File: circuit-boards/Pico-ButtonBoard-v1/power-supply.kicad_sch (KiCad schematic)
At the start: 28 parts, among them Q1 BSS123, Q2 BSS123, U2 TPS54202DDC, U6 ITS41k0S-ME-N

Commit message: Add power over CAN to supply joystick from button interfaces.
Signed-off-by: Scott Berman <sgberman1@gmail.com>
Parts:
- added D12: S1B, Diode_SMD:D_SMA, symbol Pico-ButtonBoard:S1B
- TP1: renamed from TP2; value CAN_RX -> 5V
- TP2: renamed from TP1; value CAN_RX -> VPS
- TP3: value CAN_RX -> VBAT
- renumbered D13 to D14, D16 to D17, D17 to D18, D18 to D19, D22 to D23, D23 to D24, R24 to R23, R23 to R51
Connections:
- net V_PS: now also D12.2 (A); no longer C1.1, R19.2, U2.3 (VIN)
- new net: C1.1, D12.1 (K), R19.2, U2.3 (VIN)
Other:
- note added: "5.18V Setpoint"
- note removed: "5.4V Setpoint"
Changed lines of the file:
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@@
 	(title_block
 		(title "Pico Button Board")
-		(date "2025-12-29")
+		(date "2025-12-30")
 		(rev "1")
 	)
@@
 		)
 	)
-	(text "5.4V Setpoint"
+	(text "5.18V Setpoint"
 		(exclude_from_sim no)
 		(at 279.654 147.32 0)
@@
 	)
 	(junction
+		(at 184.15 96.52)
+		(diameter 0)
+		(color 0 0 0 0)
+	)
+	(junction
 		(at 269.24 137.16)
 		(diameter 0)
@@
 	(wire
 		(pts
+			(xy 184.15 96.52) (xy 184.15 120.65)
+		)
+		(stroke
+			(width 0)
+			(type default)
+		)
+	)
+	(wire
+		(pts
 			(xy 146.05 144.78) (xy 148.59 144.78)
 		)
@@
 	(wire
 		(pts
-			(xy 184.15 93.98) (xy 184.15 120.65)
+			(xy 184.15 93.98) (xy 184.15 96.52)
 		)
 		(stroke
@@
 	(wire
 		(pts
-			(xy 184.15 120.65) (xy 210.82 120.65)
+			(xy 184.15 120.65) (xy 196.85 120.65)
 		)
 		(stroke
@@
 	(wire
 		(pts
+			(xy 184.15 96.52) (xy 349.25 96.52)
+		)
+		(stroke
+			(width 0)
+			(type default)
+		)
+	)
+	(wire
+		(pts
 			(xy 237.49 125.73) (xy 237.49 143.51)
 		)
@@
 	(wire
 		(pts
+			(xy 204.47 120.65) (xy 210.82 120.65)
+		)
+		(stroke
+			(width 0)
+			(type default)
+		)
+	)
+	(wire
+		(pts
 			(xy 102.87 139.7) (xy 102.87 144.78)
 		)
@@
 	)
 	(label "V_PS"
-		(at 193.04 120.65 0)
+		(at 185.42 120.65 0)
 		(effects
 			(font
@@
 		)
 	)
+	(hierarchical_label "V_PS"
+		(shape passive)
+		(at 349.25 96.52 0)
+		(effects
+			(font
+				(size 1.27 1.27)
+			)
+			(justify left)
+		)
+	)
 	(hierarchical_label "+V_BAT"
 		(shape input)
@@
 		(on_board yes)
 		(dnp no)
-		(property "Reference" "D13"
+		(property "Reference" "D14"
 			(at 112.268 152.4 90)
 			(effects
@@
 			(project "Pico-ButtonBoard-v1"
 				(path "/644201a9-3a2f-4df3-9c93-2ae55394df4b/dd046a3a-8e17-4277-b6b1-7e4df1560d2f"
-					(reference "D13")
+					(reference "D14")
 					(unit 1)
 				)
@@
 		(on_board yes)
 		(dnp no)
-		(property "Reference" "D16"
+		(property "Reference" "D17"
 			(at 68.072 117.602 0)
 			(effects
@@
 		)
 		(property "Value" "S1B"
-			(at 72.644 122.174 0)
+			(at 68.58 123.952 0)
 			(effects
 				(font
@@
 			(project ""
 				(path "/644201a9-3a2f-4df3-9c93-2ae55394df4b/dd046a3a-8e17-4277-b6b1-7e4df1560d2f"
-					(reference "D16")
+					(reference "D17")
 					(unit 1)
 				)
@@
 		(on_board yes)
 		(dnp no)
-		(property "Reference" "D17"
+		(property "Reference" "D18"
 			(at 68.072 90.932 0)
 			(effects
@@
 		)
 		(property "Value" "S1B"
-			(at 72.39 96.012 0)
+			(at 68.326 97.79 0)
 			(effects
 				(font
@@
 			(project "Pico-ButtonBoard-v1"
 				(path "/644201a9-3a2f-4df3-9c93-2ae55394df4b/dd046a3a-8e17-4277-b6b1-7e4df1560d2f"
-					(reference "D17")
+					(reference "D18")
+					(unit 1)
+				)
+			)
+		)
+	)
+	(symbol
+		(lib_id "Pico-ButtonBoard:S1B")
+		(at 200.66 120.65 180)
+		(unit 1)
+		(exclude_from_sim no)
+		(in_bom yes)
+		(on_board yes)
+		(dnp no)
+		(property "Reference" "D12"
+			(at 200.152 117.602 0)
+			(effects
+				(font
+					(size 1.27 1.27)
+				)
+			)
+		)
+		(property "Value" "S1B"
+			(at 200.66 123.952 0)
+			(effects
+				(font
+					(size 1.27 1.27)
+				)
+			)
+		)
+		(property "Footprint" "Diode_SMD:D_SMA"
+			(at 200.66 116.205 0)
+			(effects
+				(font
+					(size 1.27 1.27)
+				)
+				(hide yes)
+			)
+		)
+		(property "Datasheet" "Components/onsemi-S1B.pdf"
+			(at 200.66 120.65 0)
+			(effects
+				(font
+					(size 1.27 1.27)
+				)
+				(hide yes)
+			)
+		)
+		(property "Description" "100V, 1A, General Purpose Rectifier Diode, SMA(DO-214AC)"
+			(at 200.66 120.65 0)
+			(effects
+				(font
+					(size 1.27 1.27)
+				)
+				(hide yes)
+			)
+		)
+		(property "MFG" "onsemi"
+			(at 200.66 120.65 0)
+			(effects
+				(font
+					(size 1.27 1.27)
+				)
+				(hide yes)
+			)
+		)
+		(property "MFG P/N" "S1B"
+			(at 200.66 120.65 0)
+			(effects
+				(font
+					(size 1.27 1.27)
+				)
+				(hide yes)
+			)
+		)
+		(property "DIST" "Digikey"
+			(at 200.66 120.65 0)
+			(effects
+				(font
+					(size 1.27 1.27)
+				)
+				(hide yes)
+			)
+		)
+		(property "DIST P/N" "S1BFSCT-ND"
+			(at 200.66 120.65 0)
+			(effects
+				(font
+					(size 1.27 1.27)
+				)
+				(hide yes)
+			)
+		)
+		(pin "1"
+		)
+		(pin "2"
+		)
+		(instances
+			(project "Pico-ButtonBoard-v1"
+				(path "/644201a9-3a2f-4df3-9c93-2ae55394df4b/dd046a3a-8e17-4277-b6b1-7e4df1560d2f"
+					(reference "D12")
 					(unit 1)
 				)
@@
 		(on_board yes)
 		(dnp no)
-		(property "Reference" "D22"
+		(property "Reference" "D23"
 			(at 147.828 152.4 90)
 			(effects
@@
 			(project "Pico-ButtonBoard-v1"
 				(path "/644201a9-3a2f-4df3-9c93-2ae55394df4b/dd046a3a-8e17-4277-b6b1-7e4df1560d2f"
-					(reference "D22")
+					(reference "D23")
 					(unit 1)
 				)
@@
 		)
 		(property "Value" "S1B"
-			(at 339.344 124.714 0)
+			(at 335.28 126.492 0)
 			(effects
 				(font
@@
 			)
 		)
-		(property "Value" "CAN_RX"
+		(property "Value" "VBAT"
 			(at 123.19 118.6179 0)
 			(effects
@@
 		(on_board yes)
 		(dnp yes)
-		(property "Reference" "TP1"
+		(property "Reference" "TP2"
 			(at 184.15 88.646 0)
 			(effects
@@
 			)
 		)
-		(property "Value" "CAN_RX"
+		(property "Value" "VPS"
 			(at 186.69 91.9479 0)
 			(effects
@@
 			(project "Pico-ButtonBoard-v1"
 				(path "/644201a9-3a2f-4df3-9c93-2ae55394df4b/dd046a3a-8e17-4277-b6b1-7e4df1560d2f"
-					(reference "TP1")
+					(reference "TP2")
 					(unit 1)
 				)
@@
 		(on_board yes)
 		(dnp yes)
-		(property "Reference" "TP2"
+		(property "Reference" "TP1"
 			(at 316.23 117.856 0)
 			(effects
@@
 			)
 		)
-		(property "Value" "CAN_RX"
+		(property "Value" "5V"
 			(at 318.77 121.1579 0)
 			(effects
@@
 			(project "Pico-ButtonBoard-v1"
 				(path "/644201a9-3a2f-4df3-9c93-2ae55394df4b/dd046a3a-8e17-4277-b6b1-7e4df1560d2f"
-					(reference "TP2")
+					(reference "TP1")
 					(unit 1)
 				)
@@
 		(on_board yes)
 		(dnp no)
-		(property "Reference" "R23"
+		(property "Reference" "R51"
 			(at 139.954 133.35 90)
 			(effects
@@
 			(project "Pico-ButtonBoard-v1"
 				(path "/644201a9-3a2f-4df3-9c93-2ae55394df4b/dd046a3a-8e17-4277-b6b1-7e4df1560d2f"
-					(reference "R23")
+					(reference "R51")
 					(unit 1)
 				)
@@
 		(on_board yes)
 		(dnp no)
-		(property "Reference" "D18"
+		(property "Reference" "D19"
 			(at 68.072 99.822 0)
 			(effects
@@
 		)
 		(property "Value" "S1B"
-			(at 72.39 104.648 0)
+			(at 68.326 106.426 0)
 			(effects
 				(font
@@
 			(project "Pico-ButtonBoard-v1"
 				(path "/644201a9-3a2f-4df3-9c93-2ae55394df4b/dd046a3a-8e17-4277-b6b1-7e4df1560d2f"
-					(reference "D18")
+					(reference "D19")
 					(unit 1)
 				)
@@
 		(on_board yes)
 		(dnp no)
-		(property "Reference" "D23"
+		(property "Reference" "D24"
 			(at 100.584 134.874 90)
 			(effects
@@
 			(project "Pico-ButtonBoard-v1"
 				(path "/644201a9-3a2f-4df3-9c93-2ae55394df4b/dd046a3a-8e17-4277-b6b1-7e4df1560d2f"
-					(reference "D23")
+					(reference "D24")
 					(unit 1)
 				)
@@
 		(on_board yes)
 		(dnp no)
-		(property "Reference" "R24"
+		(property "Reference" "R23"
 			(at 104.394 157.48 90)
 			(effects
@@
 			(project "Pico-ButtonBoard-v1"
 				(path "/644201a9-3a2f-4df3-9c93-2ae55394df4b/dd046a3a-8e17-4277-b6b1-7e4df1560d2f"
-					(reference "R24")
+					(reference "R23")
 					(unit 1)
 				)

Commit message: Change diodes to schottky. Change 5V setpoint to 5.18V
Signed-off-by: Scott Berman <sgberman1@gmail.com>
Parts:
- D10, D12, D17, D18, D19: value S1B -> B340AE-13; DIST P/N S1BFSCT-ND -> B340AE-13DICT-ND; MFG onsemi -> Diodes Inc; MFG P/N S1B -> B340AE-13
- R18: value 12.4k-1%-0805 -> 13k-1%-0805; DIST P/N RMCF0805FT12K4CT-ND -> A126339CT-ND; MFG Stackpole -> TE Connectivity Passive Product; MFG P/N RMCF0805FT12K4 -> CRG0805F13K
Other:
- note added: "7.2-7.7V Setpoint"
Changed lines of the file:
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@@
 	(title_block
 		(title "Pico Button Board")
-		(date "2025-12-30")
+		(date "2025-12-31")
 		(rev "1")
 	)
@@
 		)
 	)
+	(text "7.2-7.7V Setpoint"
+		(exclude_from_sim no)
+		(at 226.822 131.826 0)
+		(effects
+			(font
+				(size 1.27 1.27)
+			)
+		)
+	)
 	(text_box "Power supply input range:  8V - 30V\n- Allows use of M12 and M18 Milwaukee battery packs.\n\n- Input power can be sourced from either a Milwaukee battery pack an AC power adapter.\n- Voltage of the battery pack may be higher than the AC adapter.\n- The battery pack is disabled from supplying power whenever the AC adapter is greater than 9V.\n- All inputs are protected from reverse polarity"
 		(exclude_from_sim no)
@@
 			)
 		)
-		(property "Value" "S1B"
+		(property "Value" "B340AE-13"
 			(at 68.58 123.952 0)
 			(effects
@@
 			)
 		)
-		(property "Datasheet" "Components/onsemi-S1B.pdf"
+		(property "Datasheet" "Components/DiodesInc-B340AE.pdf"
 			(at 68.58 120.65 0)
 			(effects
@@
 			)
 		)
-		(property "MFG" "onsemi"
+		(property "MFG" "Diodes Inc"
 			(at 68.58 120.65 0)
 			(effects
@@
 			)
 		)
-		(property "MFG P/N" "S1B"
+		(property "MFG P/N" "B340AE-13"
 			(at 68.58 120.65 0)
 			(effects
@@
 			)
 		)
-		(property "DIST P/N" "S1BFSCT-ND"
+		(property "DIST P/N" "B340AE-13DICT-ND"
 			(at 68.58 120.65 0)
 			(effects
@@
 			)
 		)
-		(property "Value" "S1B"
+		(property "Value" "B340AE-13"
 			(at 68.326 97.79 0)
 			(effects
@@
 			)
 		)
-		(property "Datasheet" "Components/onsemi-S1B.pdf"
+		(property "Datasheet" "Components/DiodesInc-B340AE.pdf"
 			(at 68.58 93.98 0)
 			(effects
@@
 			)
 		)
-		(property "MFG" "onsemi"
+		(property "MFG" "Diodes Inc"
 			(at 68.58 93.98 0)
 			(effects
@@
 			)
 		)
-		(property "MFG P/N" "S1B"
+		(property "MFG P/N" "B340AE-13"
 			(at 68.58 93.98 0)
 			(effects
@@
 			)
 		)
-		(property "DIST P/N" "S1BFSCT-ND"
+		(property "DIST P/N" "B340AE-13DICT-ND"
 			(at 68.58 93.98 0)
 			(effects
@@
 			)
 		)
-		(property "Value" "S1B"
+		(property "Value" "B340AE-13"
 			(at 200.66 123.952 0)
 			(effects
@@
 			)
 		)
-		(property "Datasheet" "Components/onsemi-S1B.pdf"
+		(property "Datasheet" "Components/DiodesInc-B340AE.pdf"
 			(at 200.66 120.65 0)
 			(effects
@@
 			)
 		)
-		(property "MFG" "onsemi"
+		(property "MFG" "Diodes Inc"
 			(at 200.66 120.65 0)
 			(effects
@@
 			)
 		)
-		(property "MFG P/N" "S1B"
+		(property "MFG P/N" "B340AE-13"
 			(at 200.66 120.65 0)
 			(effects
@@
 			)
 		)
-		(property "DIST P/N" "S1BFSCT-ND"
+		(property "DIST P/N" "B340AE-13DICT-ND"
 			(at 200.66 120.65 0)
 			(effects
@@
 			)
 		)
-		(property "Value" "S1B"
+		(property "Value" "B340AE-13"
 			(at 335.28 126.492 0)
 			(effects
@@
 			)
 		)
-		(property "Datasheet" "Components/onsemi-S1B.pdf"
+		(property "Datasheet" "Components/DiodesInc-B340AE.pdf"
 			(at 335.28 123.19 0)
 			(effects
@@
 			)
 		)
-		(property "MFG" "onsemi"
+		(property "MFG" "Diodes Inc"
 			(at 335.28 123.19 0)
 			(effects
@@
 			)
 		)
-		(property "MFG P/N" "S1B"
+		(property "MFG P/N" "B340AE-13"
 			(at 335.28 123.19 0)
 			(effects
@@
 			)
 		)
-		(property "DIST P/N" "S1BFSCT-ND"
+		(property "DIST P/N" "B340AE-13DICT-ND"
 			(at 335.28 123.19 0)
 			(effects
@@
 			)
 		)
-		(property "Value" "12.4k-1%-0805"
+		(property "Value" "13k-1%-0805"
 			(at 266.7 147.32 90)
 			(effects
@@
 			)
 		)
-		(property "MFG" "Stackpole"
+		(property "MFG" "TE Connectivity Passive Product"
 			(at 269.24 147.32 0)
 			(effects
@@
 			)
 		)
-		(property "MFG P/N" "RMCF0805FT12K4"
+		(property "MFG P/N" "CRG0805F13K"
 			(at 269.24 147.32 0)
 			(effects
@@
 			)
 		)
-		(property "DIST P/N" "RMCF0805FT12K4CT-ND"
+		(property "DIST P/N" "A126339CT-ND"
 			(at 269.24 147.32 0)
 			(effects
@@
 			)
 		)
-		(property "Value" "S1B"
+		(property "Value" "B340AE-13"
 			(at 68.326 106.426 0)
 			(effects
@@
 			)
 		)
-		(property "Datasheet" "Components/onsemi-S1B.pdf"
+		(property "Datasheet" "Components/DiodesInc-B340AE.pdf"
 			(at 68.58 102.87 0)
 			(effects
@@
 			)
 		)
-		(property "MFG" "onsemi"
+		(property "MFG" "Diodes Inc"
 			(at 68.58 102.87 0)
 			(effects
@@
 			)
 		)
-		(property "MFG P/N" "S1B"
+		(property "MFG P/N" "B340AE-13"
 			(at 68.58 102.87 0)
 			(effects
@@
 			)
 		)
-		(property "DIST P/N" "S1BFSCT-ND"
+		(property "DIST P/N" "B340AE-13DICT-ND"
 			(at 68.58 102.87 0)
 			(effects

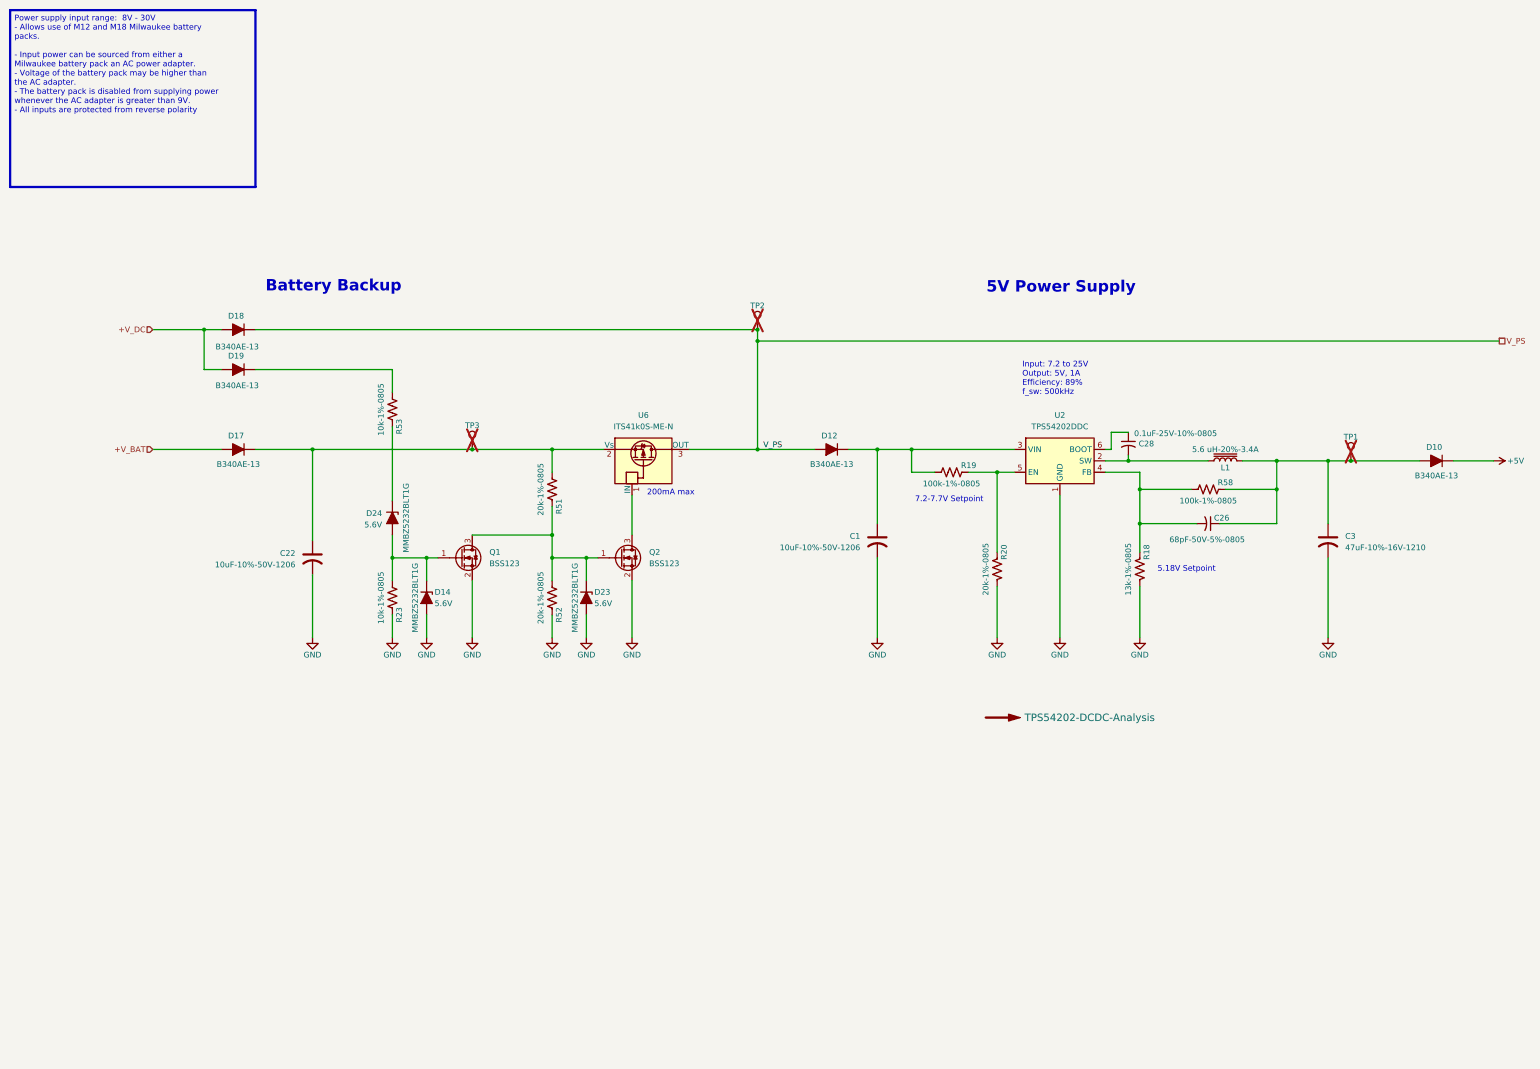
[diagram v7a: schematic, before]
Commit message: Added power indicator to button board
Signed-off-by: Scott Berman <sgberman1@gmail.com>
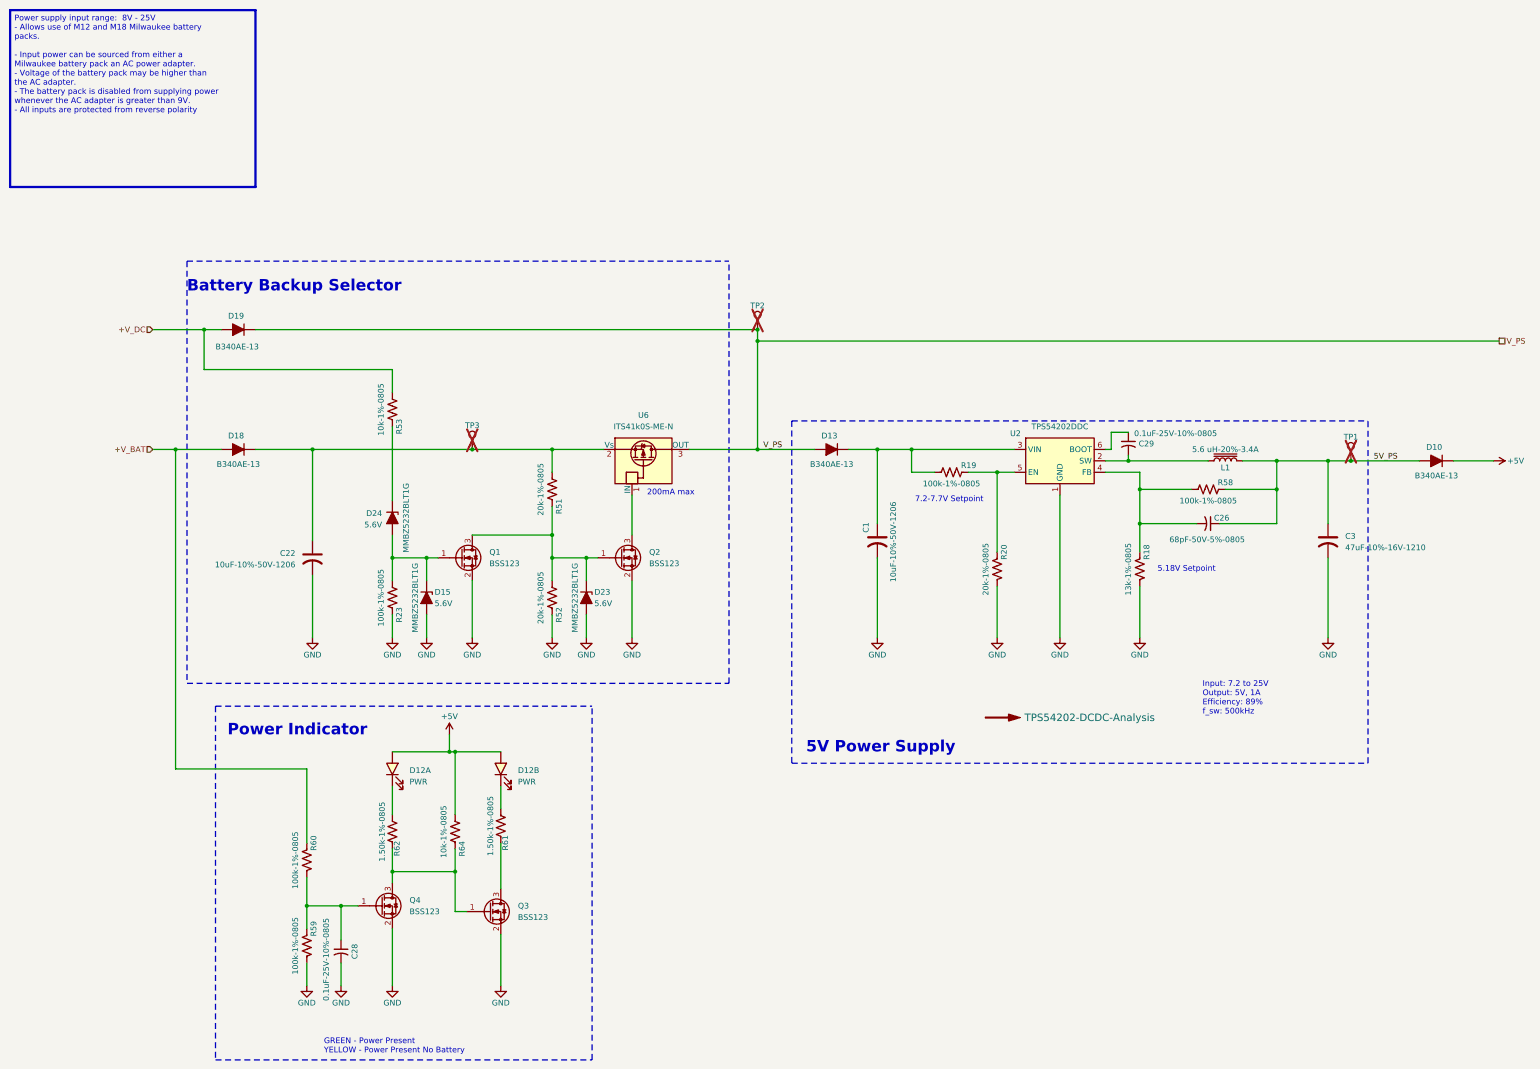
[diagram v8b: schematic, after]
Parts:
- removed D19: B340AE-13, Diode_SMD:D_SMA, symbol Pico-ButtonBoard:S1B
- added C28: 0.1uF-25V-10%-0805, Capacitor_SMD:C_0805_2012Metric_Pad1.18x1.45mm_HandSolder, symbol Device:C_Small_US
- added D12: PWR, Pico-ButtonBoard:Broadcom-HSMF-C158-LED, symbol Pico-ButtonBoard:Broadcom-DualLED-HSMF-C158
- added Q3, Q4: BSS123, Package_TO_SOT_SMD:SOT-23-3, symbol Pico-ButtonBoard:BSS123
- added R59, R60: 100k-1%-0805, Resistor_SMD:R_0805_2012Metric_Pad1.20x1.40mm_HandSolder, symbol Device:R_US
- added R61, R62: 1.50k-1%-0805, Resistor_SMD:R_0805_2012Metric_Pad1.20x1.40mm_HandSolder, symbol Device:R_US
- added R64: 10k-1%-0805, Resistor_SMD:R_0805_2012Metric_Pad1.20x1.40mm_HandSolder, symbol Device:R_US
- R23: value 10k-1%-0805 -> 100k-1%-0805; DIST P/N 541-10.0KCCT-ND -> 311-100KCRCT-ND; MFG Vishay Dale -> YAGEO; MFG P/N CRCW080510K0FKEA -> RC0805FR-07100KL
- renumbered C28 to C29, D12 to D13, D14 to D15, D17 to D18, D18 to D19
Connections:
- net +5V: now also D12.1 (AG), D12.3 (AY), R64.2
- net +V_BAT: now also R60.1
- net +V_DC: now also R53.2
- net GND: now also C28.2, Q3.2 (S), Q4.2 (S), R59.2
- net 5V_PS: now reaches C26.1, C3.1, D10.2 (A), L1.2, R58.1, TP1.1
- new net: C28.1, Q4.1 (G), R59.1, R60.2
- new net: D12.2 (KG), R62.1
- new net: Q3.1 (G), Q4.3 (D), R62.2, R64.1
- new net: Q3.3 (D), R61.2
- new net: D12.4 (KY), R61.1
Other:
- note added: "Battery Backup Selector"
- note added: "GREEN - Power Present YELLOW - Power Present No Battery"
- note added: "Power Indicator"
- note removed: "Battery Backup"
